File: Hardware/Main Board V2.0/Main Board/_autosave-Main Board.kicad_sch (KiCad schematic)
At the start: 125 parts, among them J10 Conn_01x04, J11 Conn_01x04, J12 Conn_01x04, J16 Micro_SD_Card, J6 Module A1, J6 Module A2, J6 Module A3, J6 Module B1, J6 Module B2, J6 Module B3, J7 Conn_01x04, J8 Conn_01x04, J9 Conn_01x04, Q3 MMBT2222, Q4 MMBT2222, Q5 MMBT2222, Q6 MMBT2222, SW1 SW_Push, SW2 SW_Push, U10 GT-USB-7051A, U11 AP2112K-3.3, U12 AP2112K-3.3, U5 74AHCT595, U5 ESP32-WROOM-32UE-H4, U6 74AHCT595, U6 ESP32-WROOM-32UE-H4, U7 74AHCT595, U7 CP2104, U8 74AHCT595, U8 CP2104, U9 GT-USB-7051A

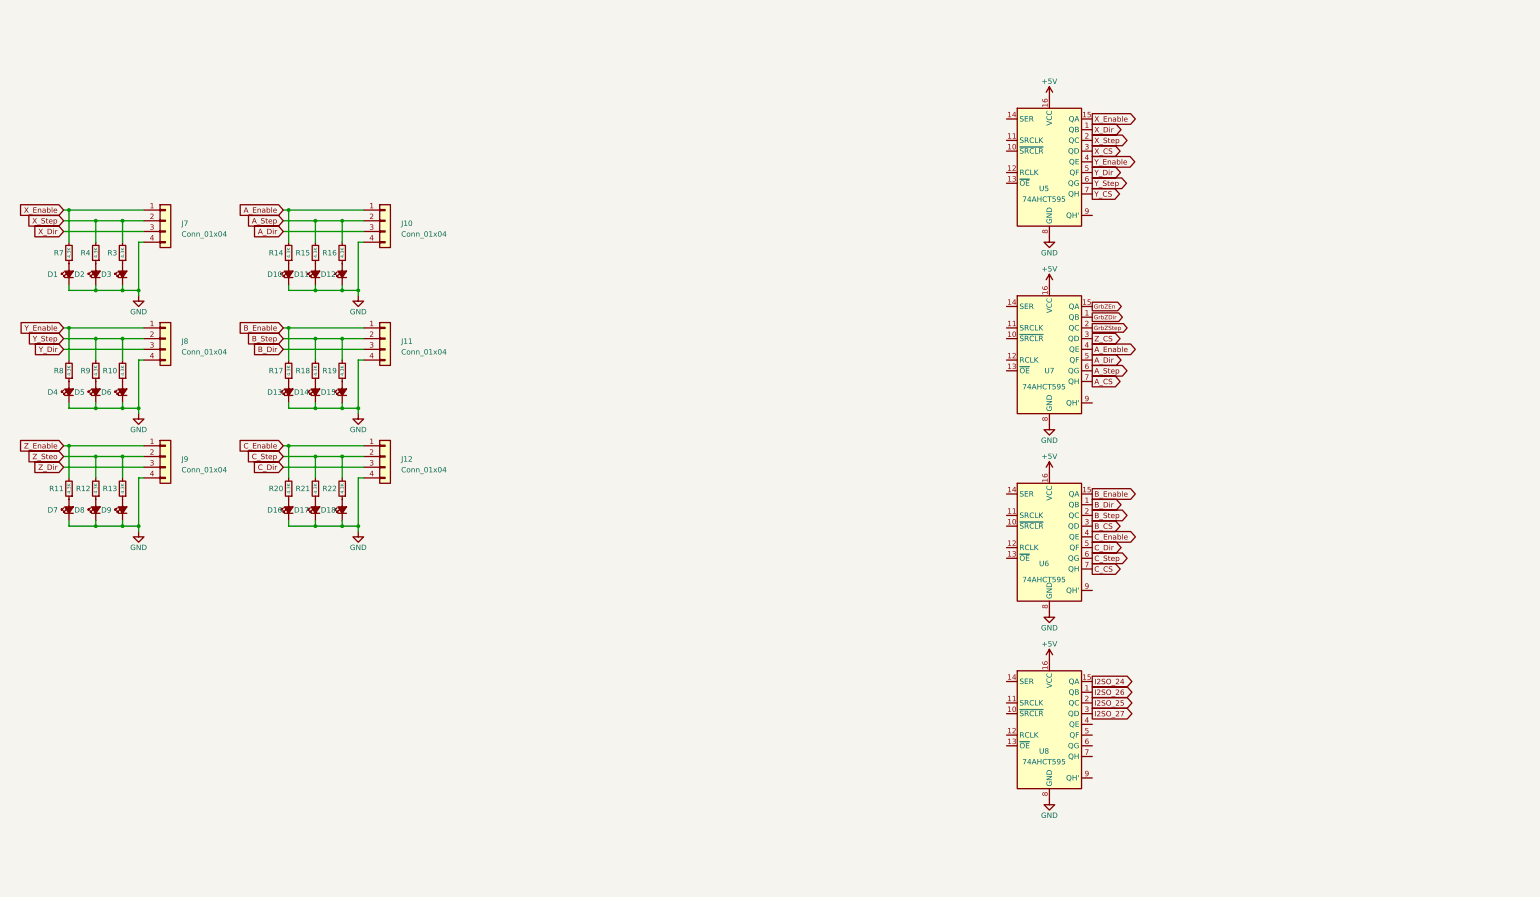
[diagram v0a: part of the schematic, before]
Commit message: Work on shift registers, and power for esp32
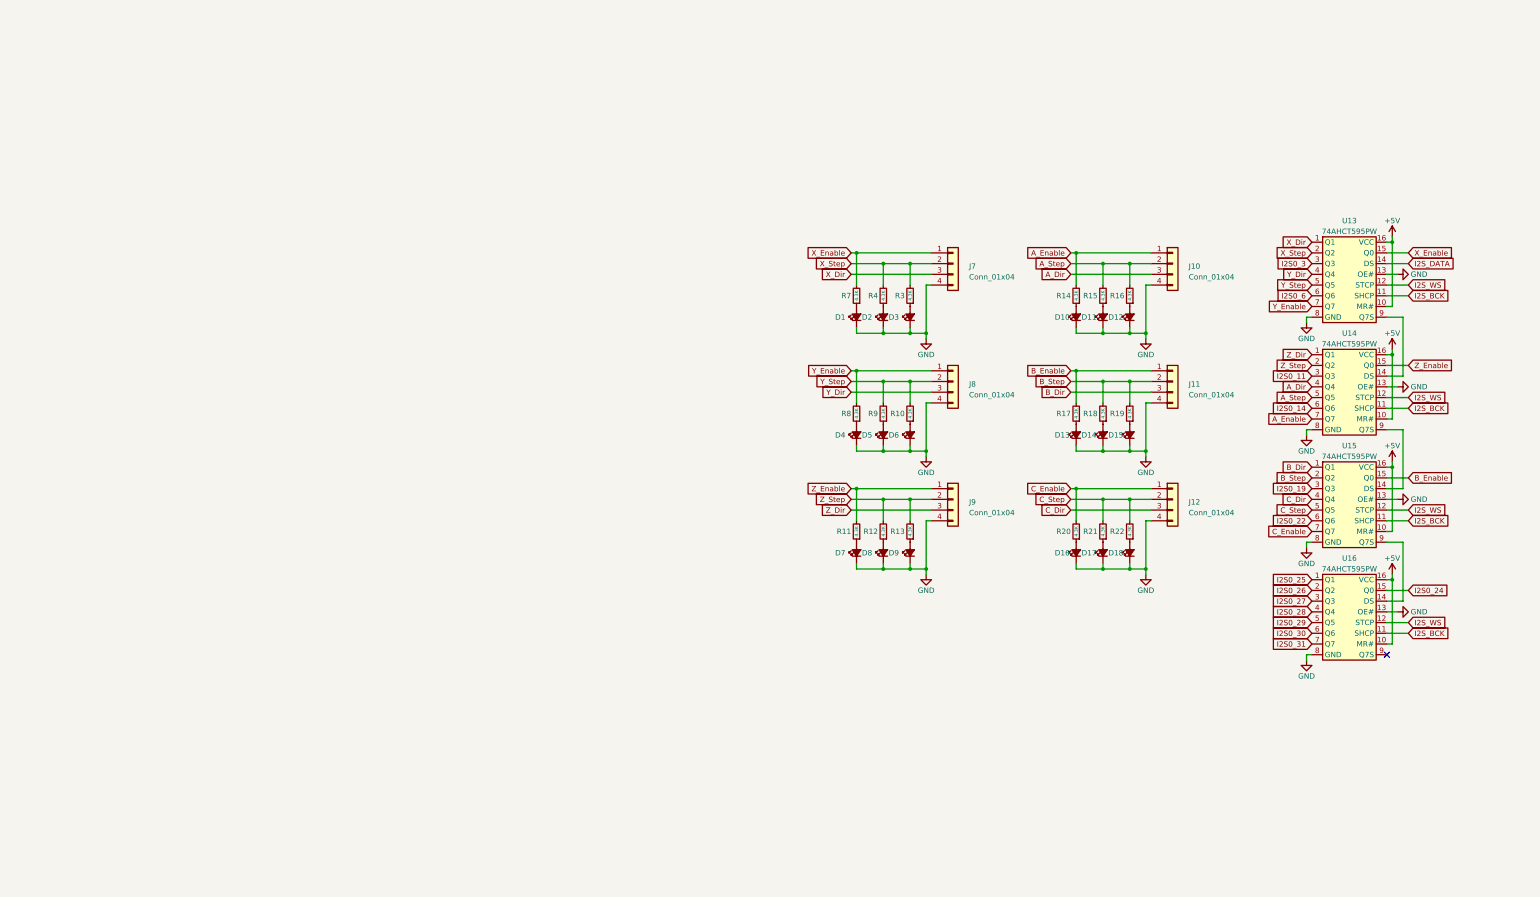
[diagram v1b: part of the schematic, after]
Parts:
- removed U5, U6, U7, U8: 74AHCT595, Package_SO:SO-16_5.3x10.2mm_P1.27mm, symbol 74xx:74AHCT595
- added U13, U14, U15, U16: 74AHCT595PW, Package_SO:TSSOP-16-1EP_4.4x5mm_P0.65mm, symbol 111_Torban_Symbols:74AHC595
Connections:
- net +5V: now also U13.10 (MR#), U13.16 (VCC), U14.10 (MR#), U14.16 (VCC), U15.10 (MR#), U15.16 (VCC), U16.10 (MR#), U16.16 (VCC)
- net A_Dir: now also U14.4 (Q4)
- net A_Enable: now also U14.7 (Q7)
- net A_Step: now also U14.5 (Q5)
- net B_Dir: now also U15.1 (Q1)
- net B_Enable: now also U15.15 (Q0)
- net B_Step: now also U15.2 (Q2)
- net C_Dir: now also U15.4 (Q4)
- net C_Enable: now also U15.7 (Q7)
- net C_Step: now also U15.5 (Q5)
- net GND: now also U13.13 (OE#), U13.8 (GND), U14.13 (OE#), U14.8 (GND), U15.13 (OE#), U15.8 (GND), U16.13 (OE#), U16.8 (GND)
- net X_Dir: now also U13.1 (Q1)
- net X_Enable: now also U13.15 (Q0)
- net X_Step: now also U13.2 (Q2)
- net Y_Dir: now also U13.4 (Q4)
- net Y_Enable: now also U13.7 (Q7)
- net Y_Step: now also U13.5 (Q5)
- net Z_Dir: now also U14.1 (Q1)
- net Z_Enable: now also U14.15 (Q0)
- net Z_Steo renamed Z_Step
- net Z_Step: now also U14.2 (Q2)
- new net: U13.9 (Q7S), U14.14 (DS)
- new net: U14.9 (Q7S), U15.14 (DS)
- new net: U15.9 (Q7S), U16.14 (DS)
- new net I2S0_11: U14.3 (Q3)
- new net I2S0_14: U14.6 (Q6)
- new net I2S0_19: U15.3 (Q3)
- new net I2S0_22: U15.6 (Q6)
- new net I2S0_24: U16.15 (Q0)
- new net I2S0_25: U16.1 (Q1)
- new net I2S0_26: U16.2 (Q2)
- new net I2S0_27: U16.3 (Q3)
- new net I2S0_28: U16.4 (Q4)
- new net I2S0_29: U16.5 (Q5)
- new net I2S0_3: U13.3 (Q3)
- new net I2S0_30: U16.6 (Q6)
- new net I2S0_31: U16.7 (Q7)
- new net I2S0_6: U13.6 (Q6)
- new net I2S_BCK: U13.11 (SHCP), U14.11 (SHCP), U15.11 (SHCP), U16.11 (SHCP)
- new net I2S_DATA: U13.14 (DS)
- new net I2S_WS: U13.12 (STCP), U14.12 (STCP), U15.12 (STCP), U16.12 (STCP)
- no-connect marks 28 -> 29
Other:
- moved on the sheet: D1, D10, D11, D12, D13, D14, D15, D16, D17, D18, D2, D3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
